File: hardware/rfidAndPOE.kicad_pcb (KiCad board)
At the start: 4 copper layers, 100 x 50 mm, 127 parts, among them J1 0813-1X1T-57-F, J2 SWD, J3 MCU Port B, J4 MCU Port C, P1 PoE-, P2 PoE+, P3 GND, P4 +5V, P5 +12V, P6 +3V3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

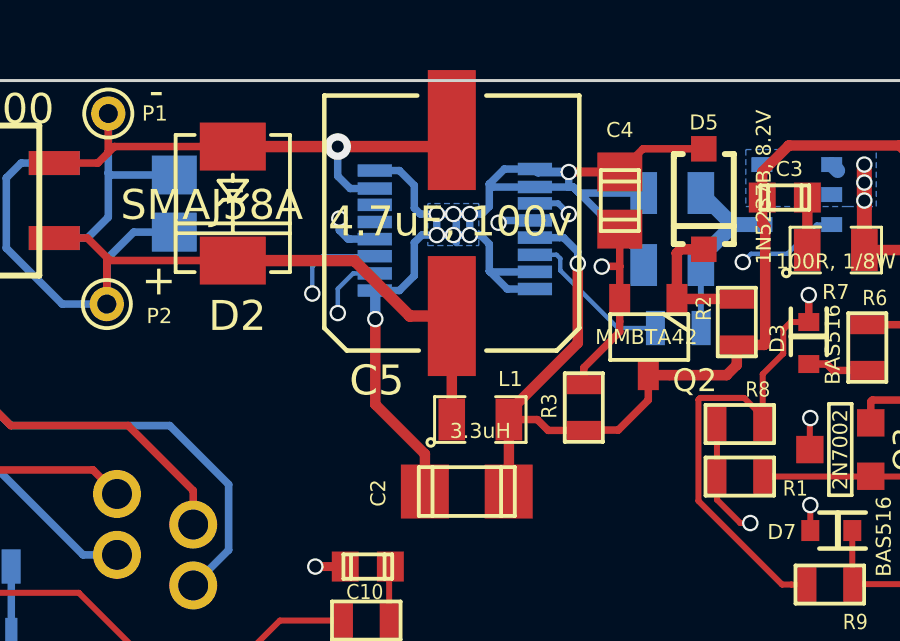
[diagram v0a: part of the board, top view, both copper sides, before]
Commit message: capacitor on input of PoE had one pad off of the board a little bit. Moved inwards.
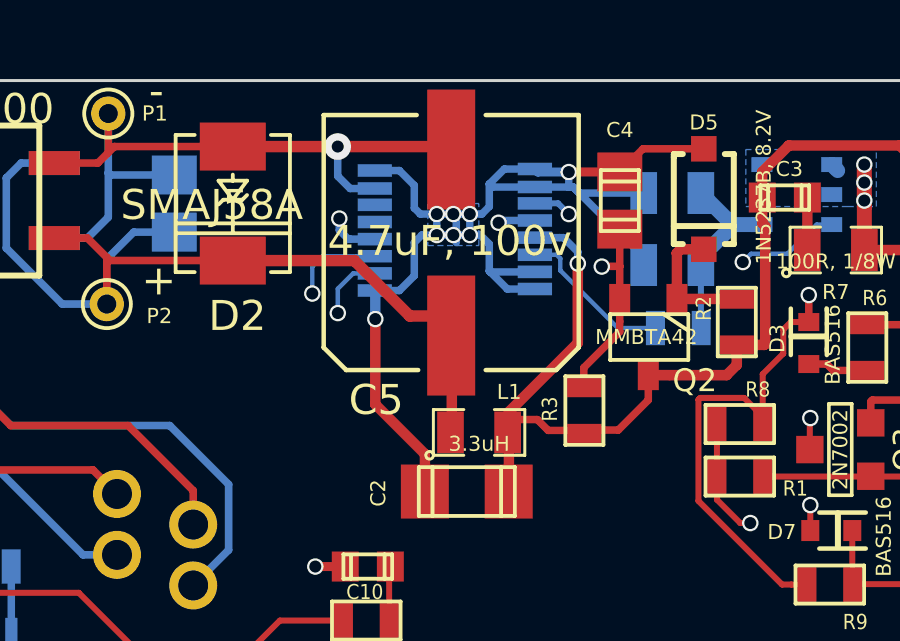
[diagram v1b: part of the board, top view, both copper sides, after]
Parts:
- moved C5 0.65 mm to (110.5, 36.1)
- moved L1 0.43 mm to (111.4, 42.4)
- moved R3 0.10 mm to (114.9, 41.7)

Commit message: Put license (CERN OHL v1.2) text on silkscreen.
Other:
- board text added: "CERN OHL v1.2"
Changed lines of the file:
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@@
     (area 57.839478 30.2 177.978572 80.750001)
     (thickness 1.6)
-    (drawings 16)
+    (drawings 17)
     (tracks 1445)
     (zones 0)
@@
     (fp_line (start 0.35052 0.89916) (end 0.7493 1.89992) (layer F.SilkS) (width 0.381))
   )
+  (gr_text "CERN OHL v1.2" (at 92.65 68.61) (layer F.SilkS)
+    (effects (font (size 1 1) (thickness 0.25)))
+  )
   (gr_text 4 (at 124.51 79.09) (layer B.Cu)

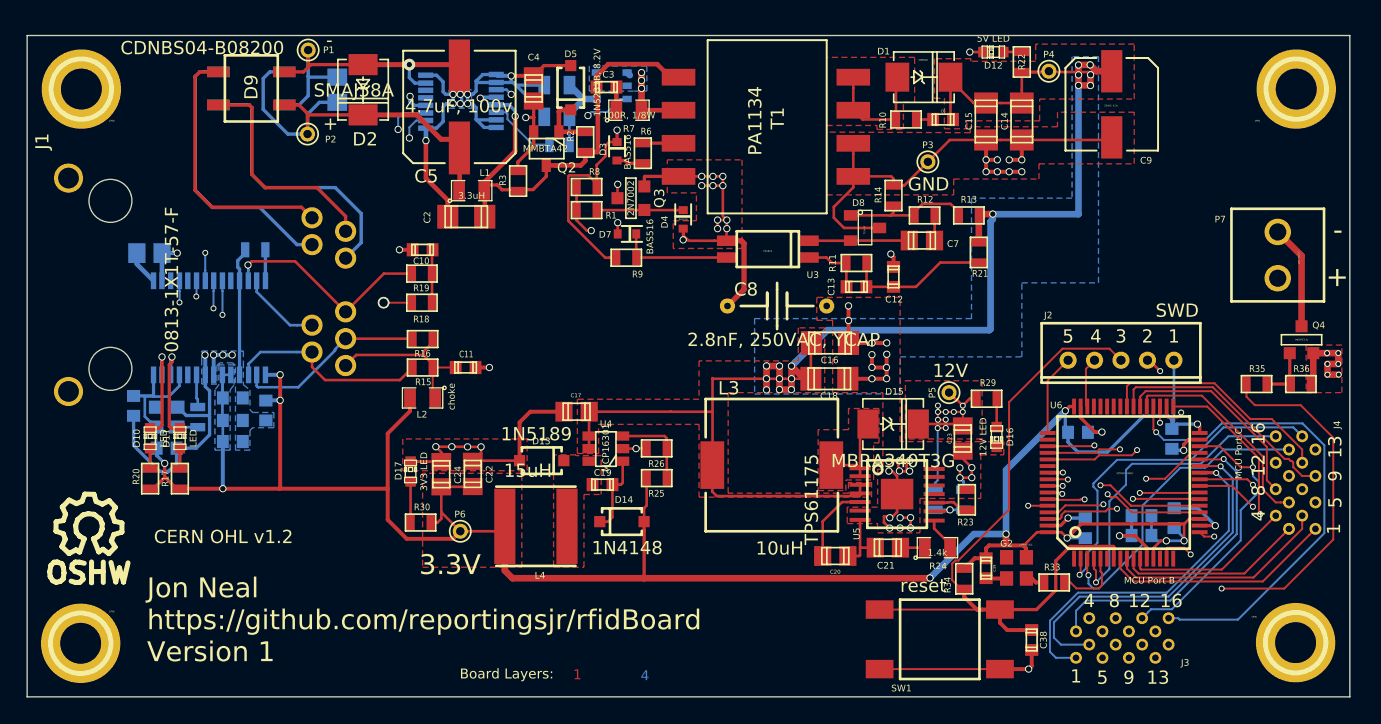
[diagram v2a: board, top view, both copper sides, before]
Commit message: Updated a bunch of silkscreen sizes and positions to make things look a little better.
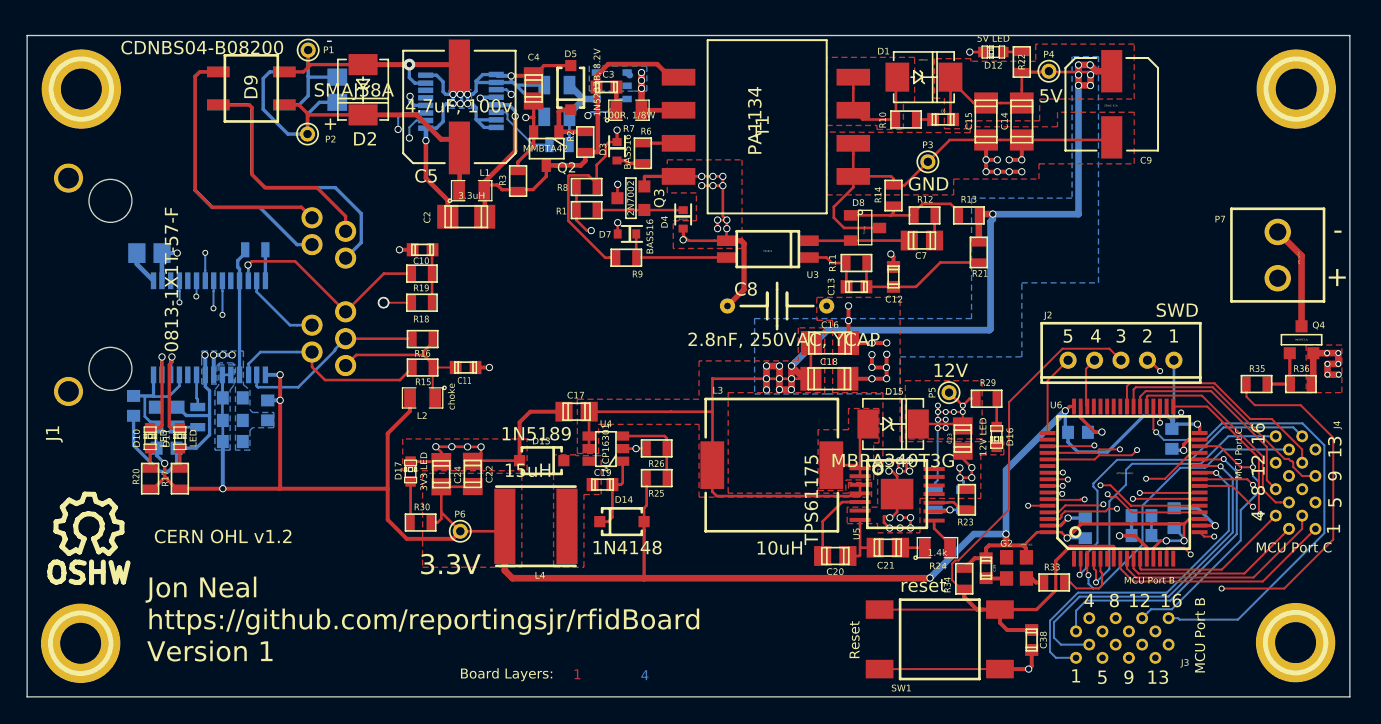
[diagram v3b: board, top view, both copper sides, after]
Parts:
- moved C28 0.14 mm to (96.0, 59.0)
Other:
- board text added: "5V"
- board text added: "MCU Port B"
- board text added: "MCU Port C"
- board text added: "Reset"

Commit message: Moved around a buch more reference designators. Also changed one trace.
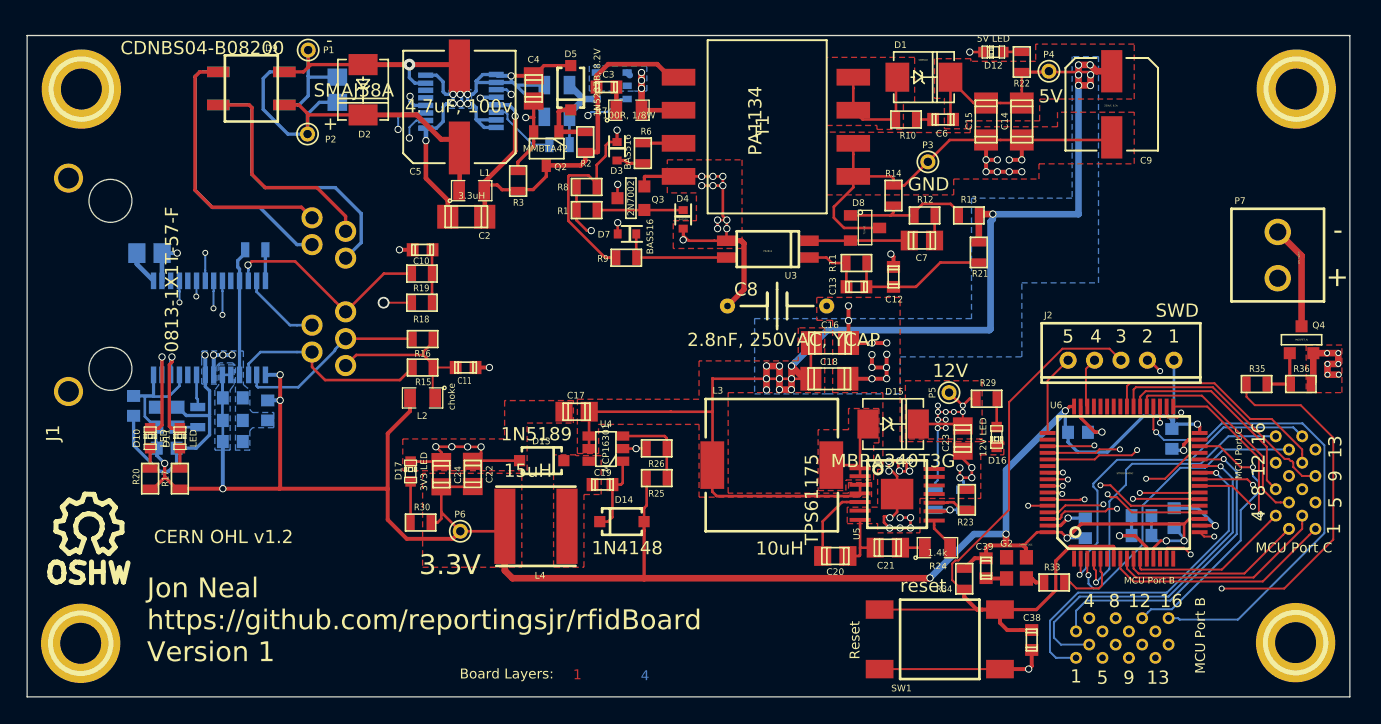
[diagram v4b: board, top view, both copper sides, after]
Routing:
- net GND: track 178.7 -> 172.1 mm

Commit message: Had to adjust size of vias and placement of silkscreen for manufacturing.
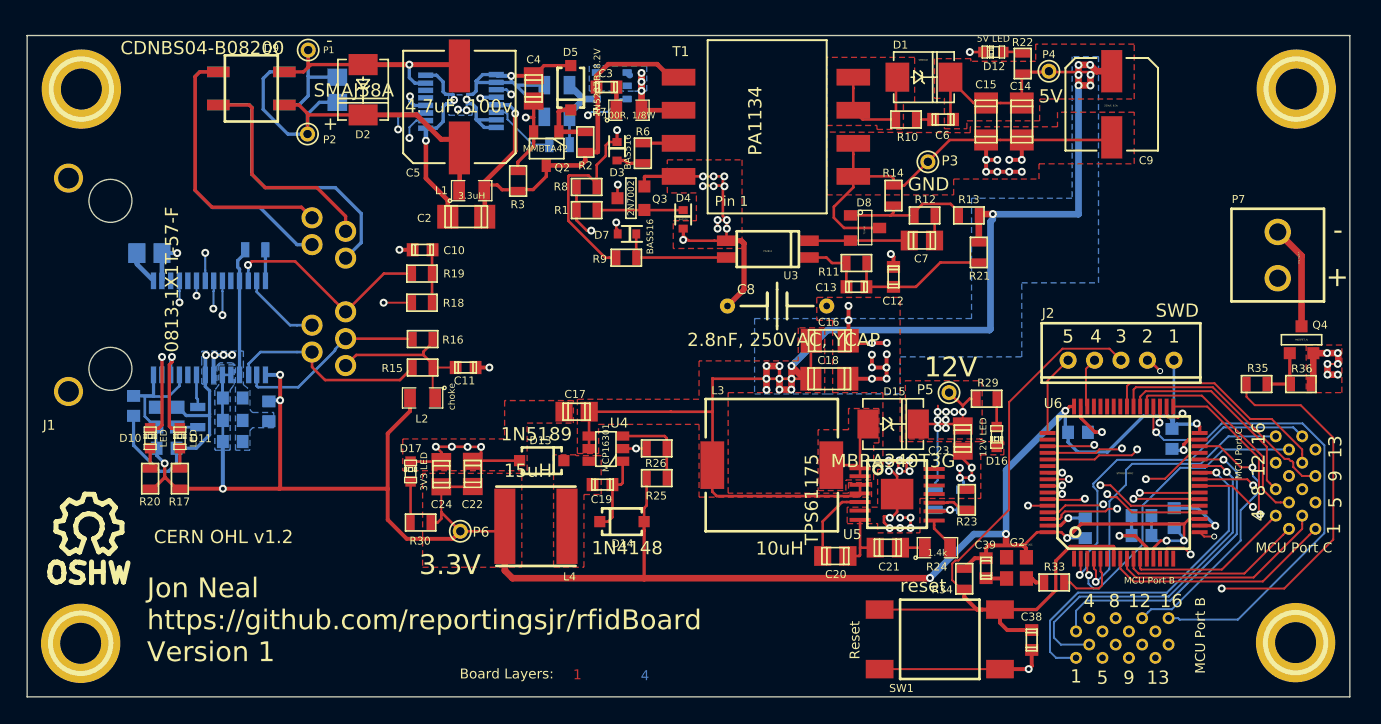
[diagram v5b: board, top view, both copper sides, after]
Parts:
- moved C16 0.18 mm to (138.5, 53.8)
- moved R22 0.14 mm to (153.1, 32.8)
- moved C28 0.11 mm to (96.1, 59.1)
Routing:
- net GNDA: track 67.9 -> 65.8 mm, vias 19 -> 17
- net 12V: vias 10 -> 8
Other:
- net class Default: via_dia 0.55 -> 0.6; via_drill 0.4 -> 0.3
